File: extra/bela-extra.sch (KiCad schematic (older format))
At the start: 22 parts, among them P1 bbbp9, P2 bbbp8, P3 enc+btn1, P4 enc+btn2, P5 MTA-156-4, P6 bela_power, U2 7805-xnor

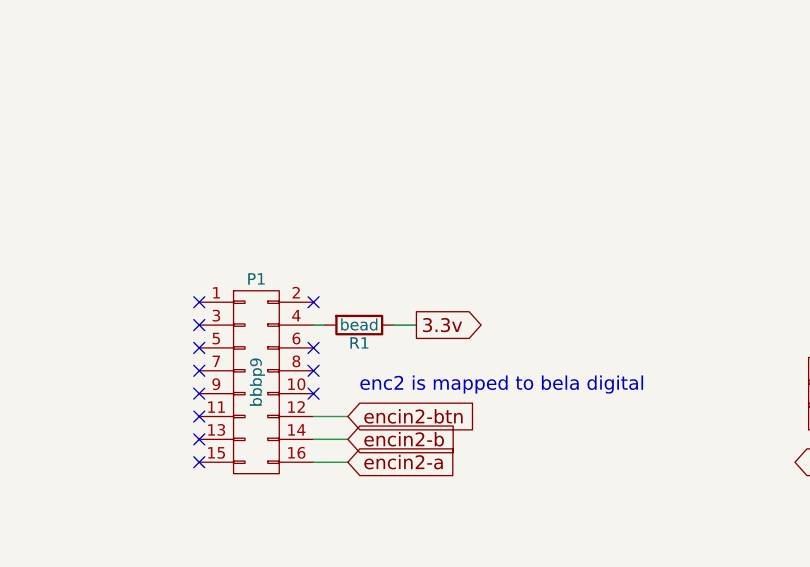
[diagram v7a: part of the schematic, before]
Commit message: 3.3v is no longer connected to 5v!
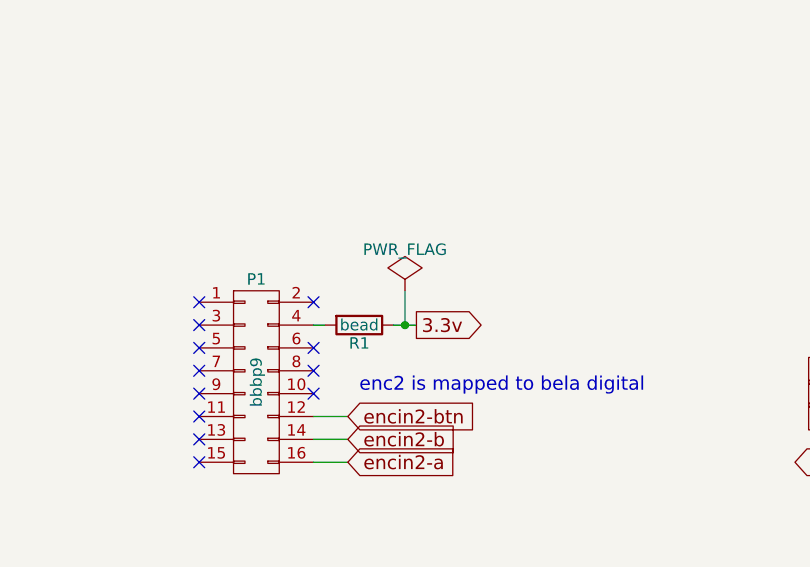
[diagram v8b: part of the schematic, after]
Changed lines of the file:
@@
 	1    0    0    -1
 $EndComp
+$Comp
+L PWR_FLAG #FLG09
+U 1 1 586F1ADD
+P 2400 3650
+F 0 "#FLG09" H 2400 3745 50  0001 C CNN
+F 1 "PWR_FLAG" H 2400 3830 50  0000 C CNN
+F 2 "" H 2400 3650 50  0000 C CNN
+F 3 "" H 2400 3650 50  0000 C CNN
+	1    2400 3650
+	1    0    0    -1
+$EndComp
+Wire Wire Line
+	2400 3650 2400 3800
+Connection ~ 2400 3800
 $EndSCHEMATC
